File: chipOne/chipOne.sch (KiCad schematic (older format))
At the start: 1 part

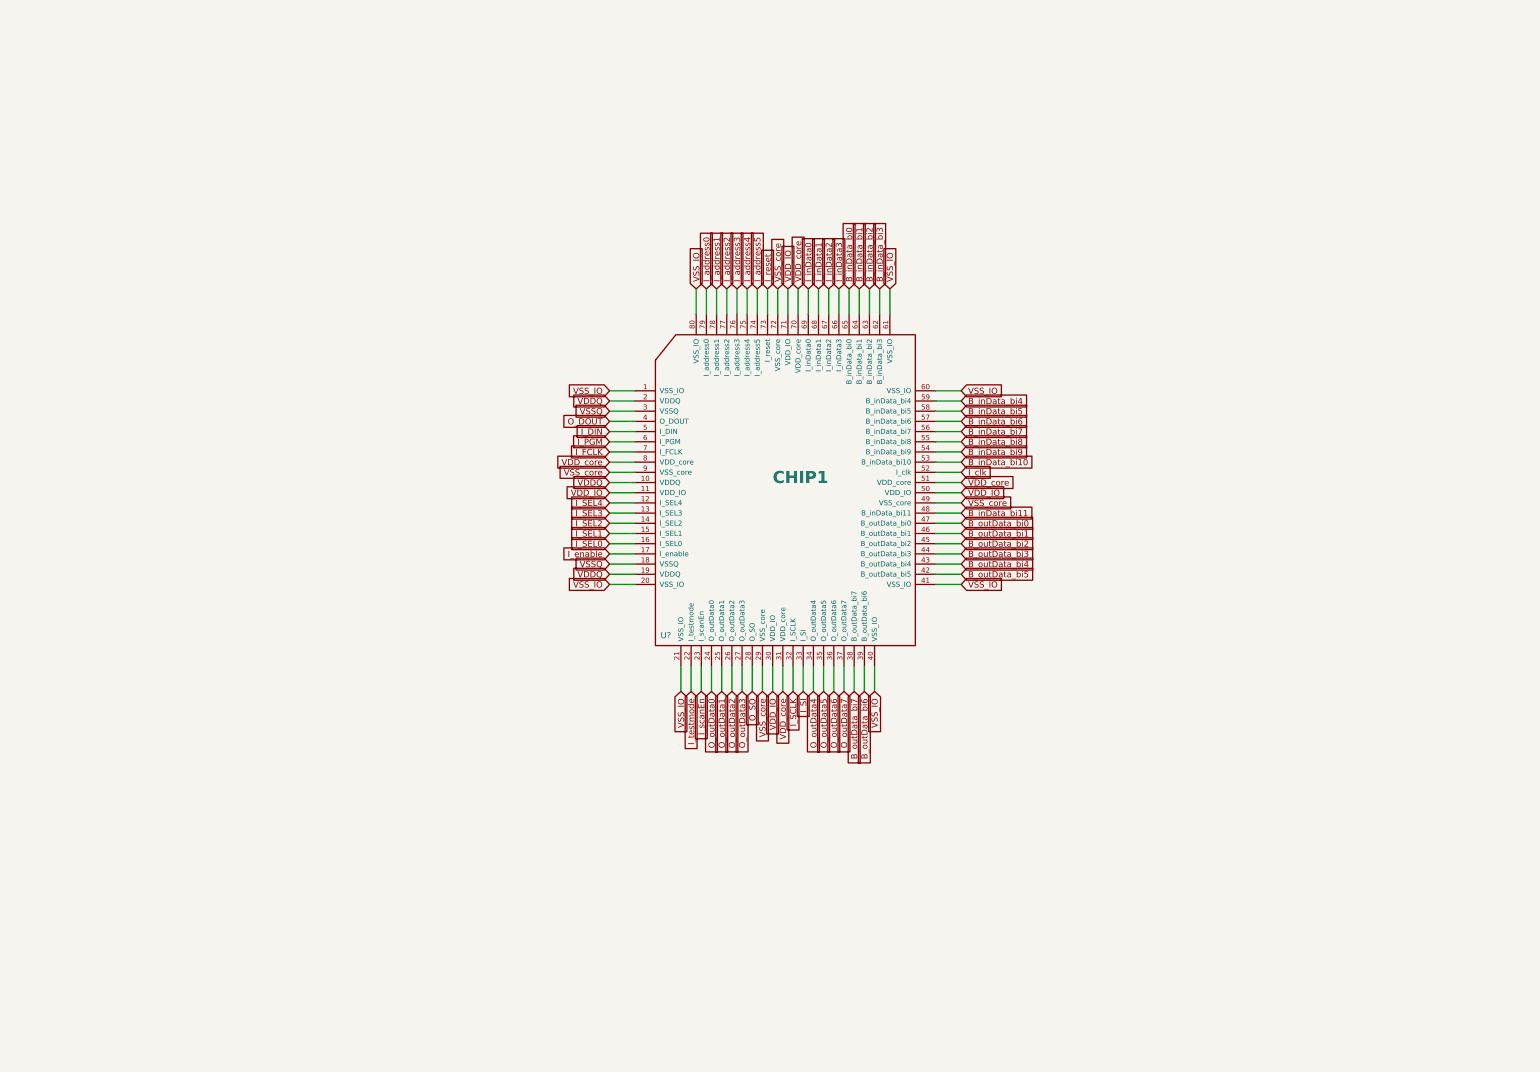
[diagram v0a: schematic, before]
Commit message: Chip pcb initial stahe and schematic completed, Generator to DUT socket and connections are made
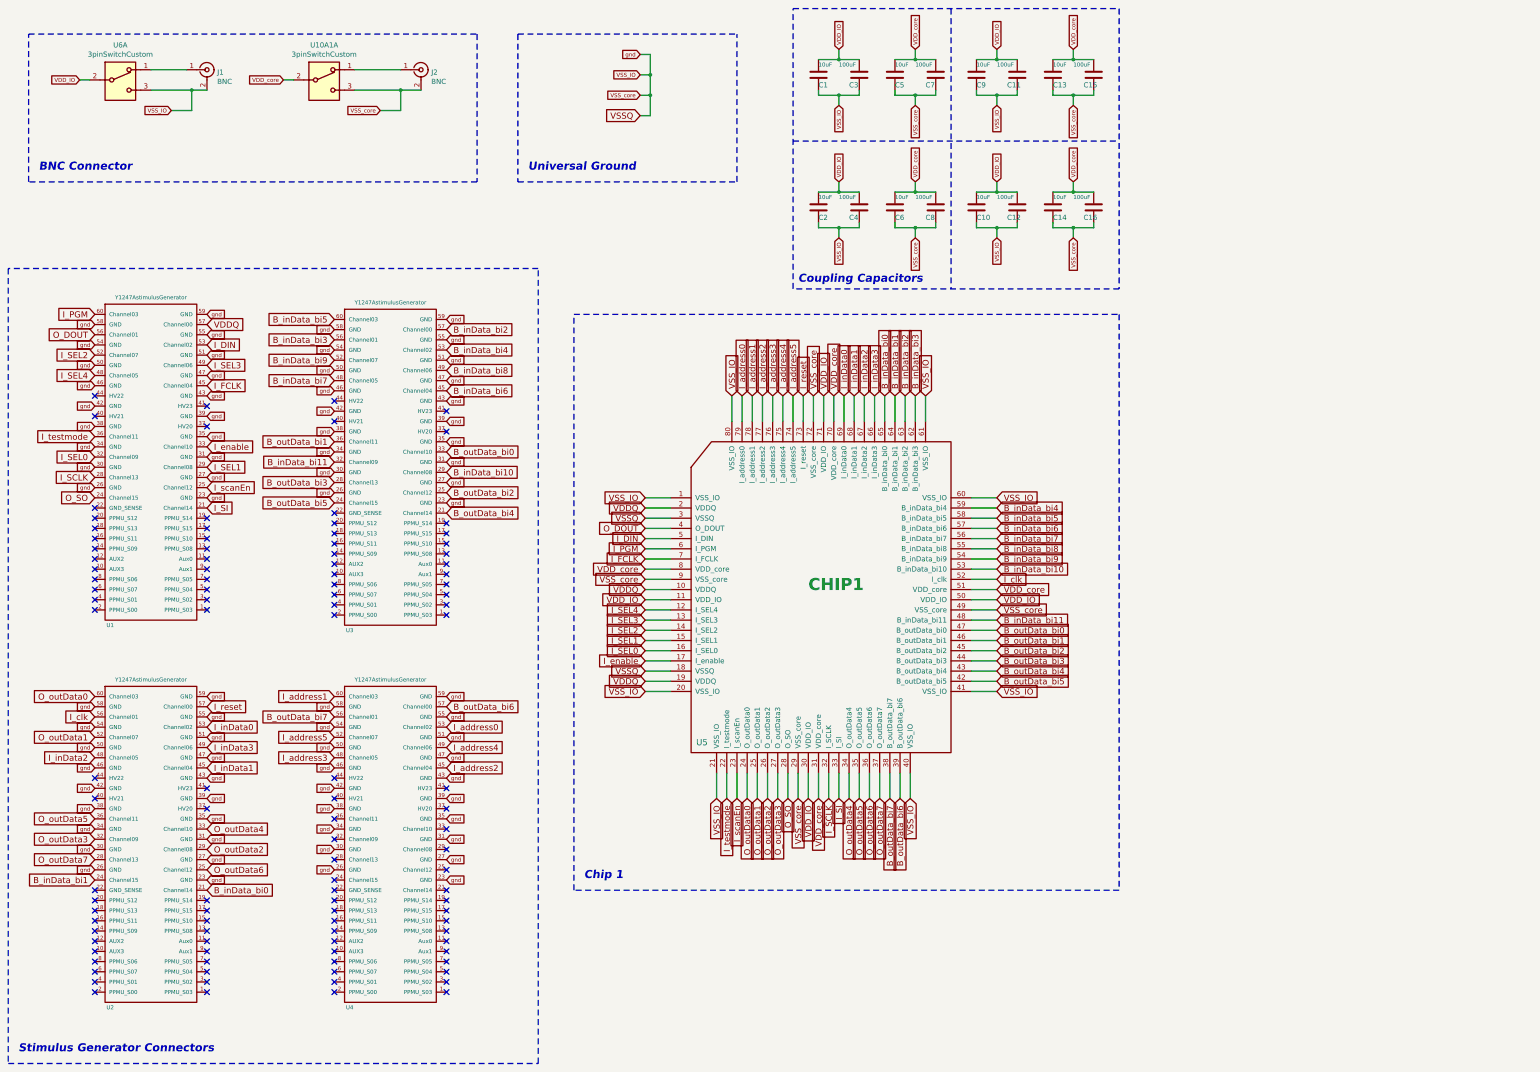
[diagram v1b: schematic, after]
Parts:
- added C1, C10, C13, C14, C2, C5, C6, C9: 10uF, Capacitors_SMD:C_1206_HandSoldering, symbol Device:C
- added C11, C12, C15, C16, C3, C4, C7, C8: 100uF, Capacitors_Tantalum_SMD:CP_Tantalum_Case-X_EIA-7343-43_Hand, symbol Device:C
- added J1, J2: BNC, bnc_connector:TE_227161-1, symbol Connector:Conn_Coaxial
- added U1, U2, U3, U4: Y1247AstimulusGenerator, Y1247AstimulusGenerator:ERF8-030-05.0-L-DV-L-TR, symbol Y1247AstimulusGenerator:Y1247AstimulusGenerator
- added U10A1, U6: 3pinSwitchCustom, Pin_Headers:Pin_Header_Straight_1x03_Pitch2.54mm, symbol 3pinSwitchCustom:3pinSwitchCustom
- U5: renamed from U?; footprint (none) -> chip1:280-5205-01
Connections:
- net VSS_IO is gone; now on net VSSQ: U5.1 (VSS_IO), U5.20 (VSS_IO), U5.21 (VSS_IO), U5.40 (VSS_IO), U5.41 (VSS_IO), U5.60 (VSS_IO), U5.61 (VSS_IO), U5.80 (VSS_IO)
- net VSS_core is gone; now on net VSSQ: U5.29 (VSS_core), U5.49 (VSS_core), U5.72 (VSS_core), U5.9 (VSS_core)
- net B_inData_bi0: now also U2.21 (Channel14)
- net B_inData_bi1: now also U2.24 (Channel15)
- net B_inData_bi10: now also U3.29 (Channel08)
- net B_inData_bi11: now also U3.32 (Channel09)
- net B_inData_bi2: now also U3.57 (Channel00)
- net B_inData_bi3: now also U3.56 (Channel01)
- net B_inData_bi4: now also U3.53 (Channel02)
- net B_inData_bi5: now also U3.60 (Channel03)
- net B_inData_bi6: now also U3.45 (Channel04)
- net B_inData_bi7: now also U3.48 (Channel05)
- net B_inData_bi8: now also U3.49 (Channel06)
- net B_inData_bi9: now also U3.52 (Channel07)
- net B_outData_bi0: now also U3.33 (Channel10)
- net B_outData_bi1: now also U3.36 (Channel11)
- net B_outData_bi2: now also U3.25 (Channel12)
- net B_outData_bi3: now also U3.28 (Channel13)
- net B_outData_bi4: now also U3.21 (Channel14)
- net B_outData_bi5: now also U3.24 (Channel15)
- net B_outData_bi6: now also U4.57 (Channel00)
- net B_outData_bi7: now also U4.56 (Channel01)
- net I_DIN: now also U1.53 (Channel02)
- net I_FCLK: now also U1.45 (Channel04)
- net I_PGM: now also U1.60 (Channel03)
- net I_SCLK: now also U1.28 (Channel13)
- net I_SEL0: now also U1.32 (Channel09)
- net I_SEL1: now also U1.29 (Channel08)
- net I_SEL2: now also U1.52 (Channel07)
- net I_SEL3: now also U1.49 (Channel06)
- net I_SEL4: now also U1.48 (Channel05)
- net I_SI: now also U1.21 (Channel14)
- net I_address0: now also U4.53 (Channel02)
- net I_address1: now also U4.60 (Channel03)
- net I_address2: now also U4.45 (Channel04)
- net I_address3: now also U4.48 (Channel05)
- net I_address4: now also U4.49 (Channel06)
- net I_address5: now also U4.52 (Channel07)
- net I_clk: now also U2.56 (Channel01)
- net I_enable: now also U1.33 (Channel10)
- net I_inData0: now also U2.53 (Channel02)
- net I_inData1: now also U2.45 (Channel04)
- net I_inData2: now also U2.48 (Channel05)
- net I_inData3: now also U2.49 (Channel06)
- net I_reset: now also U2.57 (Channel00)
- net I_scanEn: now also U1.25 (Channel12)
- net I_testmode: now also U1.36 (Channel11)
- net O_DOUT: now also U1.56 (Channel01)
- net O_SO: now also U1.24 (Channel15)
- net O_outData0: now also U2.60 (Channel03)
- net O_outData1: now also U2.52 (Channel07)
- net O_outData2: now also U2.29 (Channel08)
- net O_outData3: now also U2.32 (Channel09)
- net O_outData4: now also U2.33 (Channel10)
- net O_outData5: now also U2.36 (Channel11)
- net O_outData6: now also U2.25 (Channel12)
- net O_outData7: now also U2.28 (Channel13)
- net VDDQ: now also U1.57 (Channel00)
- net VDD_IO: now also C1.1, C10.1, C11.1, C12.1, C2.1, C3.1, C4.1, C9.1, U6.2
- net VDD_core: now also C13.1, C14.1, C15.1, C16.1, C5.1, C6.1, C7.1, C8.1, U10A1.2
- net VSSQ: now also C1.2, C10.2, C11.2, C12.2, C13.2, C14.2, C15.2, C16.2, C2.2, C3.2, C4.2, C5.2, C6.2, C7.2, C8.2, C9.2, J1.2 (Ext), J2.2 (Ext), U1.23 (GND), U1.26 (GND), U1.27 (GND), U1.30 (GND), U1.31 (GND), U1.34 (GND), U1.35 (GND), U1.38 (GND), U1.39 (GND), U1.42 (GND), U1.43 (GND), U1.46 (GND), U1.47 (GND), U1.50 (GND), U1.51 (GND), U1.54 (GND), U1.55 (GND), U1.58 (GND), U1.59 (GND), U10A1.3, U2.23 (GND), U2.26 (GND), U2.27 (GND), U2.30 (GND), U2.31 (GND), U2.34 (GND), U2.35 (GND), U2.38 (GND), U2.39 (GND), U2.42 (GND), U2.43 (GND), U2.46 (GND), U2.47 (GND), U2.50 (GND), U2.51 (GND), U2.54 (GND), U2.55 (GND), U2.58 (GND), U2.59 (GND), U3.23 (GND), U3.26 (GND), U3.27 (GND), U3.30 (GND), U3.31 (GND), U3.34 (GND), U3.35 (GND), U3.38 (GND), U3.39 (GND), U3.42 (GND), U3.43 (GND), U3.46 (GND), U3.47 (GND), U3.50 (GND), U3.51 (GND), U3.54 (GND), U3.55 (GND), U3.58 (GND), U3.59 (GND), U4.23 (GND), U4.26 (GND), U4.27 (GND), U4.30 (GND), U4.31 (GND), U4.34 (GND), U4.35 (GND), U4.38 (GND), U4.39 (GND), U4.42 (GND), U4.43 (GND), U4.46 (GND), U4.47 (GND), U4.50 (GND), U4.51 (GND), U4.54 (GND), U4.55 (GND), U4.58 (GND), U4.59 (GND), U6.3
- new net: J1.1 (In), U6.1
- new net: J2.1 (In), U10A1.1
- no-connect marks 0 -> 108
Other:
- note added: "BNC Connector"
- note added: "Chip 1"
- note added: "Coupling Capacitors"
- note added: "Stimulus Generator Connectors"
- note added: "Universal Ground"
- moved on the sheet: U5

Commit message: Stage one of Chip 1 is completed
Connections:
- net VDD_core renamed +1V0
- net VSSQ renamed GND
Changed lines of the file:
@@
 Wire Wire Line
 	4050 1500 4500 1500
-Wire Wire Line
-	1450 1400 1350 1400
-Wire Wire Line
-	3450 1400 3350 1400
 Text GLabel 3350 1400 0    39   Input ~ 0
 VDD_core
@@
 	1    0    0    -1
 $EndComp
+Wire Wire Line
+	1350 1400 1450 1400
+Wire Wire Line
+	3350 1400 3400 1400
+$Comp
+L power:GND #PWR?
+U 1 1 5EE071BC
+P 6950 1750
+F 0 "#PWR?" H 6950 1500 50  0001 C CNN
+F 1 "GND" H 6955 1577 50  0000 C CNN
+F 2 "" H 6950 1750 50  0001 C CNN
+F 3 "" H 6950 1750 50  0001 C CNN
+	1    6950 1750
+	1    0    0    -1
+$EndComp
+Connection ~ 6950 1750
+$Comp
+L power:+1V0 #PWR?
+U 1 1 5EE07C4B
+P 3400 1400
+F 0 "#PWR?" H 3400 1250 50  0001 C CNN
+F 1 "+1V0" H 3415 1573 50  0000 C CNN
+F 2 "" H 3400 1400 50  0001 C CNN
+F 3 "" H 3400 1400 50  0001 C CNN
+	1    3400 1400
+	1    0    0    -1
+$EndComp
+Connection ~ 3400 1400
+Wire Wire Line
+	3400 1400 3450 1400
 $EndSCHEMATC

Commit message: Layout for PCB one made : stage 1
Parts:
- added J3, J4: 5767007-8, U4164AlogicAnalyser:TE_5767007-8, symbol U4164AlogicAnalyser:5767007-8
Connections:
- net B_inData_bi0: now also J3.10
- net B_inData_bi1: now also J3.8
- net B_inData_bi10: now also J4.21
- net B_inData_bi11: now also J4.19
- net B_inData_bi2: now also J4.37
- net B_inData_bi3: now also J4.35
- net B_inData_bi4: now also J4.33
- net B_inData_bi5: now also J4.31
- net B_inData_bi6: now also J4.29
- net B_inData_bi7: now also J4.27
- net B_inData_bi8: now also J4.25
- net B_inData_bi9: now also J4.23
- net B_outData_bi0: now also J4.17
- net B_outData_bi1: now also J4.15
- net B_outData_bi2: now also J4.13
- net B_outData_bi3: now also J4.11
- net B_outData_bi4: now also J4.9
- net B_outData_bi5: now also J4.7
- net B_outData_bi6: now also J4.38
- net B_outData_bi7: now also J4.36
- net I_DIN: now also J3.33
- net I_FCLK: now also J3.29
- net I_PGM: now also J3.31
- net I_SCLK: now also J3.11
- net I_SEL0: now also J3.19
- net I_SEL1: now also J3.21
- net I_SEL2: now also J3.23
- net I_SEL3: now also J3.25
- net I_SEL4: now also J3.27
- net I_SI: now also J3.9
- net I_address0: now also J4.34
- net I_address1: now also J4.32
- net I_address2: now also J4.30
- net I_address3: now also J4.28
- net I_address4: now also J4.26
- net I_address5: now also J4.24
- net I_clk: now also J3.36, J3.5, J3.6, J4.5, J4.6
- net I_enable: now also J3.17
- net I_inData0: now also J3.34
- net I_inData1: now also J3.30
- net I_inData2: now also J3.28
- net I_inData3: now also J3.26
- net I_reset: now also J3.38
- net I_scanEn: now also J3.13
- net I_testmode: now also J3.15
- net O_DOUT: now also J3.35
- net O_SO: now also J3.7
- net O_outData0: now also J3.32
- net O_outData1: now also J3.24
- net O_outData2: now also J3.22
- net O_outData3: now also J3.20
- net O_outData4: now also J3.18
- net O_outData5: now also J3.16
- net O_outData6: now also J3.14
- net O_outData7: now also J3.12
- net VDDQ: now also J3.37
- net +1V0 renamed VDD_core
- net GND renamed VSSQ
- net VSSQ: now also J3.S1 (SHIELD), J3.S2 (SHIELD), J3.S3 (SHIELD), J3.S4 (SHIELD), J3.S5 (SHIELD), J4.S1 (SHIELD), J4.S2 (SHIELD), J4.S3 (SHIELD), J4.S4 (SHIELD), J4.S5 (SHIELD)
- no-connect marks 108 -> 124
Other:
- note added: "Logic Analyzer Connectors"
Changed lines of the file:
@@
 Text GLabel 6850 1750 0    60   Input ~ 0
 VSSQ
-Text GLabel 6850 1150 0    39   Input ~ 0
+Text GLabel 6850 1150 0    59   Input ~ 12
 gnd
 Text GLabel 6850 1550 0    39   Input ~ 0
@@
 P 8100 5750
 F 0 "U5" H 7400 3600 60  0000 L CNN
-F 1 "CHIP1" H 8500 5150 118 0000 L CNB
+F 1 "CHIP1" H 8400 5050 118 0000 L CNB
 F 2 "chip1:280-5205-01" H 8100 5750 60  0001 C CNN
 F 3 "" H 8100 5750 60  0001 C CNN
@@
 Wire Wire Line
 	1350 1400 1450 1400
-Wire Wire Line
-	3350 1400 3400 1400
 $Comp
-L power:GND #PWR?
-U 1 1 5EE071BC
-P 6950 1750
-F 0 "#PWR?" H 6950 1500 50  0001 C CNN
-F 1 "GND" H 6955 1577 50  0000 C CNN
-F 2 "" H 6950 1750 50  0001 C CNN
-F 3 "" H 6950 1750 50  0001 C CNN
-	1    6950 1750
+L U4164AlogicAnalyser:5767007-8 J3
+U 1 1 5EDFE2BC
+P 13850 5050
+F 0 "J3" H 13850 6315 50  0000 C CNN
+F 1 "5767007-8" H 13850 6224 50  0000 C CNN
+F 2 "U4164AlogicAnalyser:TE_5767007-8" H 13850 5050 50  0001 L BNN
+F 3 "Compliant" H 13850 5050 50  0001 L BNN
+F 4 "5767007-8" H 13850 5050 50  0001 L BNN "Field4"
+F 5 "Connector" H 13850 5050 50  0001 L BNN "Field5"
+F 6 "38" H 13850 5050 50  0001 L BNN "Field6"
+F 7 ".64" H 13850 5050 50  0001 L BNN "Field7"
+	1    13850 5050
 	1    0    0    -1
 $EndComp
-Connection ~ 6950 1750
+Text GLabel 14350 4250 2    60   Input ~ 0
+I_clk
+Text GLabel 14350 4350 2    60   Input ~ 0
+B_inData_bi1
+Text GLabel 14350 4450 2    60   Input ~ 0
+B_inData_bi0
+Text GLabel 14350 4550 2    60   Input ~ 0
+O_outData7
+Text GLabel 14350 4650 2    60   Input ~ 0
+O_outData6
+Text GLabel 14350 4750 2    60   Input ~ 0
+O_outData5
+Text GLabel 14350 4850 2    60   Input ~ 0
+O_outData4
+Text GLabel 14350 4950 2    60   Input ~ 0
+O_outData3
+Text GLabel 14350 5050 2    60   Input ~ 0
+O_outData2
+Text GLabel 14350 5150 2    60   Input ~ 0
+O_outData1
+Text GLabel 14350 5250 2    60   Input ~ 0
+I_inData3
+Text GLabel 14350 5350 2    60   Input ~ 0
+I_inData2
+Text GLabel 14350 5450 2    60   Input ~ 0
+I_inData1
+Text GLabel 14350 5550 2    60   Input ~ 0
+O_outData0
+Text GLabel 14350 5650 2    60   Input ~ 0
+I_inData0
+Text GLabel 14350 5750 2    60   Input ~ 0
+I_clk
+Text GLabel 14350 5850 2    60   Input ~ 0
+I_reset
+Text GLabel 13350 5850 0    60   Input ~ 0
+VDDQ
+Text GLabel 13350 5750 0    60   Input ~ 0
+O_DOUT
+Text GLabel 13350 5650 0    60   Input ~ 0
+I_DIN
+Text GLabel 13350 5550 0    60   Input ~ 0
+I_PGM
+Text GLabel 13350 5450 0    60   Input ~ 0
+I_FCLK
+Text GLabel 13350 5350 0    60   Input ~ 0
+I_SEL4
+Text GLabel 13350 5250 0    60   Input ~ 0
+I_SEL3
+Text GLabel 13350 5150 0    60   Input ~ 0
+I_SEL2
+Text GLabel 13350 5050 0    60   Input ~ 0
+I_SEL1
+Text GLabel 13350 4950 0    60   Input ~ 0
+I_SEL0
+Text GLabel 13350 4850 0    60   Input ~ 0
+I_enable
+Text GLabel 13350 4750 0    60   Input ~ 0
+I_testmode
+Text GLabel 13350 4650 0    60   Input ~ 0
+I_scanEn
+Text GLabel 13350 4550 0    60   Input ~ 0
+I_SCLK
+Text GLabel 13350 4450 0    60   Input ~ 0
+I_SI
+Text GLabel 13350 4350 0    60   Input ~ 0
+O_SO
+Text GLabel 13350 4250 0    60   Input ~ 0
+I_clk
+Text GLabel 14350 6050 2    39   Input ~ 0
+gnd
+NoConn ~ 14350 4150
+NoConn ~ 14350 4050
+NoConn ~ 13350 4150
+NoConn ~ 13350 4050
+Wire Wire Line
+	3350 1400 3450 1400
 $Comp
-L power:+1V0 #PWR?
-U 1 1 5EE07C4B
-P 3400 1400
-F 0 "#PWR?" H 3400 1250 50  0001 C CNN
-F 1 "+1V0" H 3415 1573 50  0000 C CNN
-F 2 "" H 3400 1400 50  0001 C CNN
-F 3 "" H 3400 1400 50  0001 C CNN
-	1    3400 1400
+L U4164AlogicAnalyser:5767007-8 J4
+U 1 1 5EE04108
+P 13850 7950
+F 0 "J4" H 13850 9215 50  0000 C CNN
+F 1 "5767007-8" H 13850 9124 50  0000 C CNN
+F 2 "U4164AlogicAnalyser:TE_5767007-8" H 13850 7950 50  0001 L BNN
+F 3 "Compliant" H 13850 7950 50  0001 L BNN
+F 4 "5767007-8" H 13850 7950 50  0001 L BNN "Field4"
+F 5 "Connector" H 13850 7950 50  0001 L BNN "Field5"
+F 6 "38" H 13850 7950 50  0001 L BNN "Field6"
+F 7 ".64" H 13850 7950 50  0001 L BNN "Field7"
+	1    13850 7950
 	1    0    0    -1
 $EndComp
-Connection ~ 3400 1400
-Wire Wire Line
-	3400 1400 3450 1400
+Text GLabel 13350 7150 0    60   Input ~ 0
+I_clk
+Text GLabel 14350 7150 2    60   Input ~ 0
+I_clk
+Text GLabel 14350 8050 2    60   Input ~ 0
+I_address5
+Text GLabel 14350 8150 2    60   Input ~ 0
+I_address4
+Text GLabel 14350 8250 2    60   Input ~ 0
+I_address3
+Text GLabel 14350 8350 2    60   Input ~ 0
+I_address2
+Text GLabel 14350 8450 2    60   Input ~ 0
+I_address1
+Text GLabel 14350 8550 2    60   Input ~ 0
+I_address0
+Text GLabel 14350 8650 2    60   Input ~ 0
+B_outData_bi7
+Text GLabel 14350 8750 2    60   Input ~ 0
+B_outData_bi6
+Text GLabel 13350 8750 0    60   Input ~ 0
+B_inData_bi2
+Text GLabel 13350 8650 0    60   Input ~ 0
+B_inData_bi3
+Text GLabel 13350 8550 0    60   Input ~ 0
+B_inData_bi4
+Text GLabel 13350 8450 0    60   Input ~ 0
+B_inData_bi5
+Text GLabel 13350 8350 0    60   Input ~ 0
+B_inData_bi6
+Text GLabel 13350 8150 0    60   Input ~ 0
+B_inData_bi8
+Text GLabel 13350 8250 0    60   Input ~ 0
+B_inData_bi7
+Text GLabel 13350 8050 0    60   Input ~ 0
+B_inData_bi9
+Text GLabel 13350 7950 0    60   Input ~ 0
+B_inData_bi10
+Text GLabel 13350 7850 0    60   Input ~ 0
+B_inData_bi11
+Text GLabel 13350 7750 0    60   Input ~ 0
+B_outData_bi0
+Text GLabel 13350 7650 0    60   Input ~ 0
+B_outData_bi1
+Text GLabel 13350 7550 0    60   Input ~ 0
+B_outData_bi2
+Text GLabel 13350 7450 0    60   Input ~ 0
+B_outData_bi3
+Text GLabel 13350 7350 0    60   Input ~ 0
+B_outData_bi4
+Text GLabel 13350 7250 0    60   Input ~ 0
+B_outData_bi5
+Text GLabel 14350 8950 2    39   Input ~ 0
+gnd
+NoConn ~ 14350 6950
+NoConn ~ 14350 7050
+NoConn ~ 13350 7050
+NoConn ~ 13350 6950
+NoConn ~ 14350 7250
+NoConn ~ 14350 7350
+NoConn ~ 14350 7450
+NoConn ~ 14350 7550
+NoConn ~ 14350 7650
+NoConn ~ 14350 7950
+NoConn ~ 14350 7850
+NoConn ~ 14350 7750
+Wire Notes Line
+	12050 3700 15600 3700
+Wire Notes Line
+	15600 3700 15600 9350
+Wire Notes Line
+	15600 9350 12050 9350
+Wire Notes Line
+	12050 9350 12050 3700
+Text Notes 12150 9250 0    79   Italic 16
+Logic Analyzer Connectors
 $EndSCHEMATC

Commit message: Chip Two design and schematic completed
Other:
- note added: "Logic Analyzer Connectors (U4205)"
- note added: "Stimulus Generator Connectors (Y1247A)"
- note removed: "Logic Analyzer Connectors"
- note removed: "Stimulus Generator Connectors"
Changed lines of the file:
@@
 BNC Connector
 Text Notes 750  10950 0    79   Italic 16
-Stimulus Generator Connectors
+Stimulus Generator Connectors  (Y1247A)
 Wire Notes Line
 	11550 9350 6200 9350
@@
 	12050 9350 12050 3700
 Text Notes 12150 9250 0    79   Italic 16
-Logic Analyzer Connectors
+Logic Analyzer Connectors (U4205)
 $EndSCHEMATC

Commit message: Switch changed in both the layout
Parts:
- U10A1, U6: footprint Pin_Headers:Pin_Header_Straight_1x03_Pitch2.54mm -> SW_MS12ANW03:SW_MS12ANW03
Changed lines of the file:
@@
 F 0 "U6" H 1750 1542 50  0000 C CNN
 F 1 "3pinSwitchCustom" H 1750 1451 50  0000 C CNN
-F 2 "Pin_Headers:Pin_Header_Straight_1x03_Pitch2.54mm" H 1800 950 50  0001 C CNN
+F 2 "SW_MS12ANW03:SW_MS12ANW03" H 1800 950 50  0001 C CNN
 F 3 "http://www.ti.com/lit/ds/symlink/ts5a3159.pdf" H 1750 1300 50  0001 C CNN
 	1    1750 1300
@@
 F 0 "U10A1" H 3750 1542 50  0000 C CNN
 F 1 "3pinSwitchCustom" H 3750 1451 50  0000 C CNN
-F 2 "Pin_Headers:Pin_Header_Straight_1x03_Pitch2.54mm" H 3800 950 50  0001 C CNN
+F 2 "SW_MS12ANW03:SW_MS12ANW03" H 3800 950 50  0001 C CNN
 F 3 "http://www.ti.com/lit/ds/symlink/ts5a3159.pdf" H 3750 1300 50  0001 C CNN
 	1    3750 1300
